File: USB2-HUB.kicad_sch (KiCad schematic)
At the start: 31 parts, among them J15 USB_OTG, J16 690-008-221-904, U12 FSUSB42MUX, U13 USB2514B-I/M2, U14 TPD4EUSB30, U15 AP22653W6, Y3 24MHz

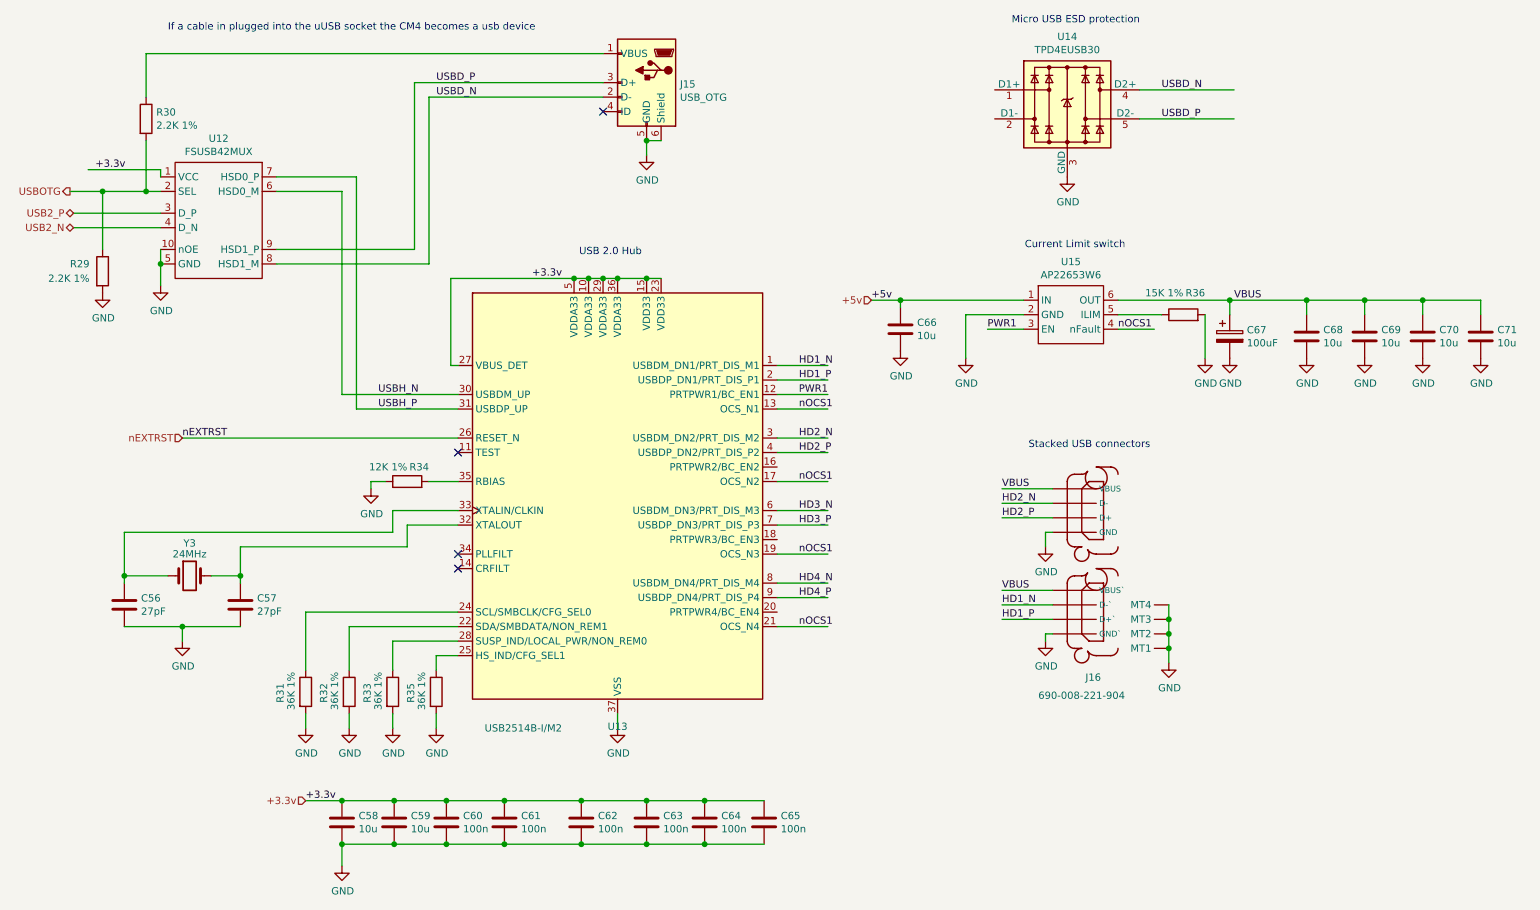
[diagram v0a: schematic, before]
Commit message: Initial layout and all parts added. Some pins still not connected to power
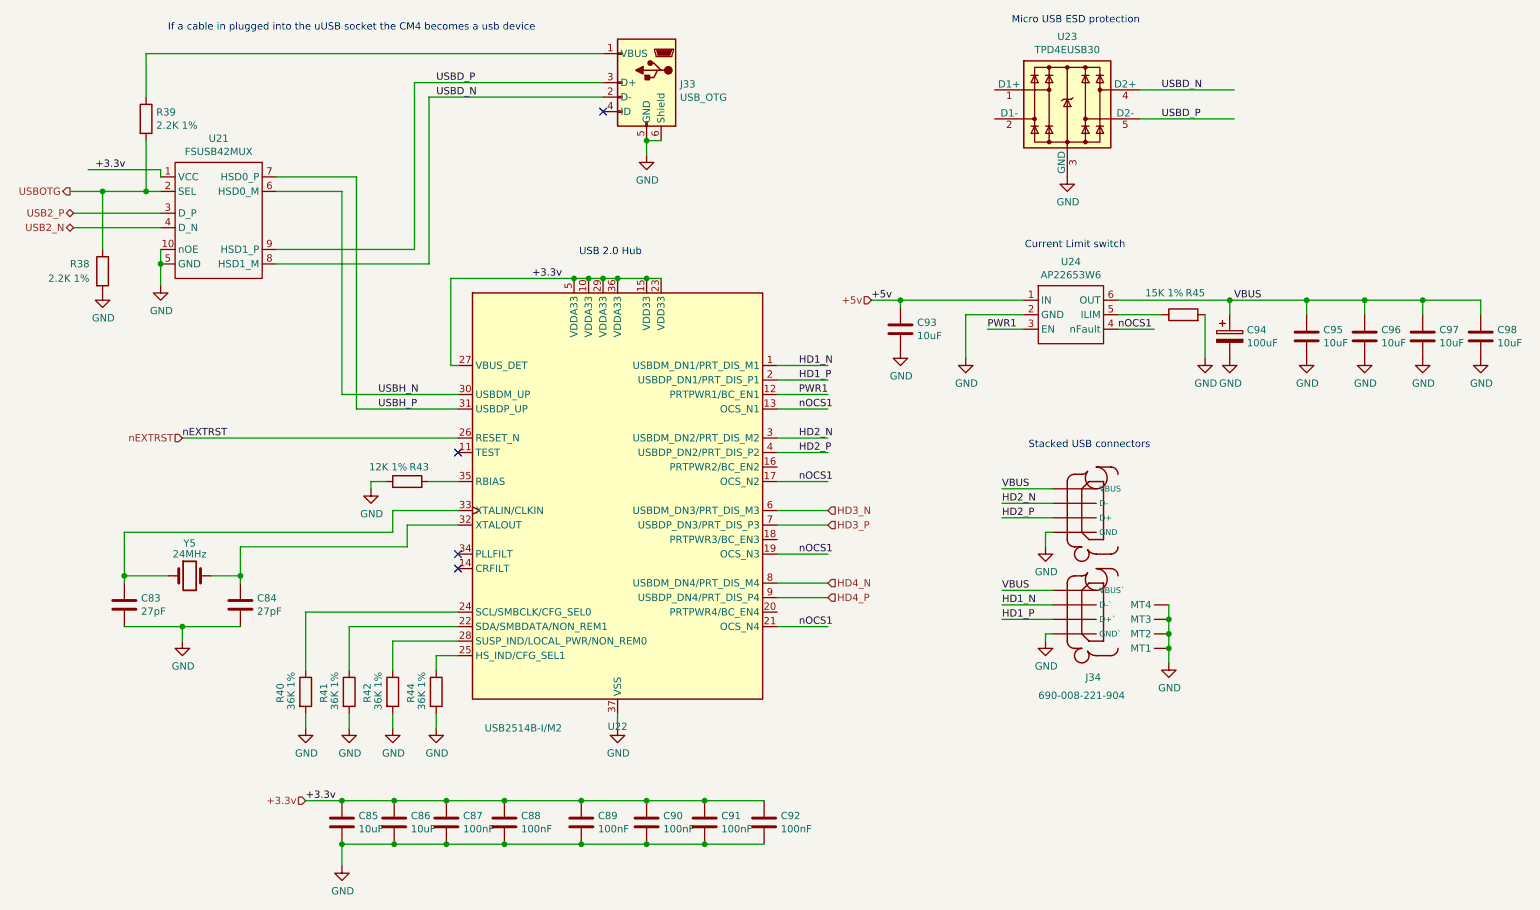
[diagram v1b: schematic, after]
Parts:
- C85: renamed from C58; value 10u -> 10uF
- C86: renamed from C59; value 10u -> 10uF
- C87: renamed from C60; value 100n -> 100nF
- C88: renamed from C61; value 100n -> 100nF
- C89: renamed from C62; value 100n -> 100nF
- C90: renamed from C63; value 100n -> 100nF
- C91: renamed from C64; value 100n -> 100nF
- C92: renamed from C65; value 100n -> 100nF
- C93: renamed from C66; value 10u -> 10uF
- C95: renamed from C68; value 10u -> 10uF
- C96: renamed from C69; value 10u -> 10uF
- C97: renamed from C70; value 10u -> 10uF
- C98: renamed from C71; value 10u -> 10uF
- Y5: renamed from Y3; footprint Crystal:Crystal_SMD_HC49-SD -> Crystal:Crystal_SMD_2012-2Pin_2.0x1.2mm
- renumbered C56 to C83, C57 to C84, C67 to C94, J15 to J33, J16 to J34, R29 to R38, R30 to R39, R31 to R40, R32 to R41, R33 to R42, R34 to R43, R35 to R44, R36 to R45, U12 to U21, U13 to U22, U14 to U23, U15 to U24

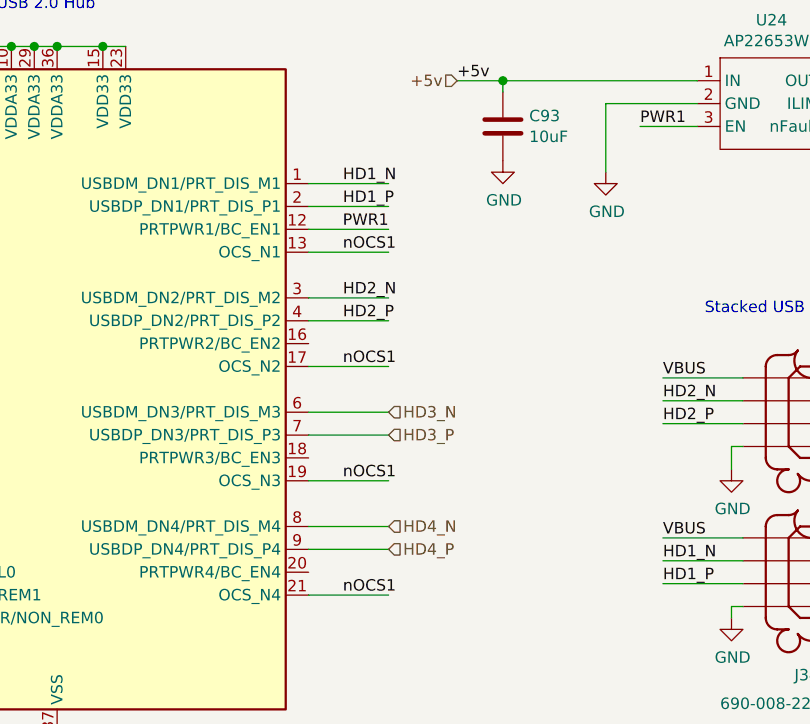
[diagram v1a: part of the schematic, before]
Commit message: Diff pairs routed
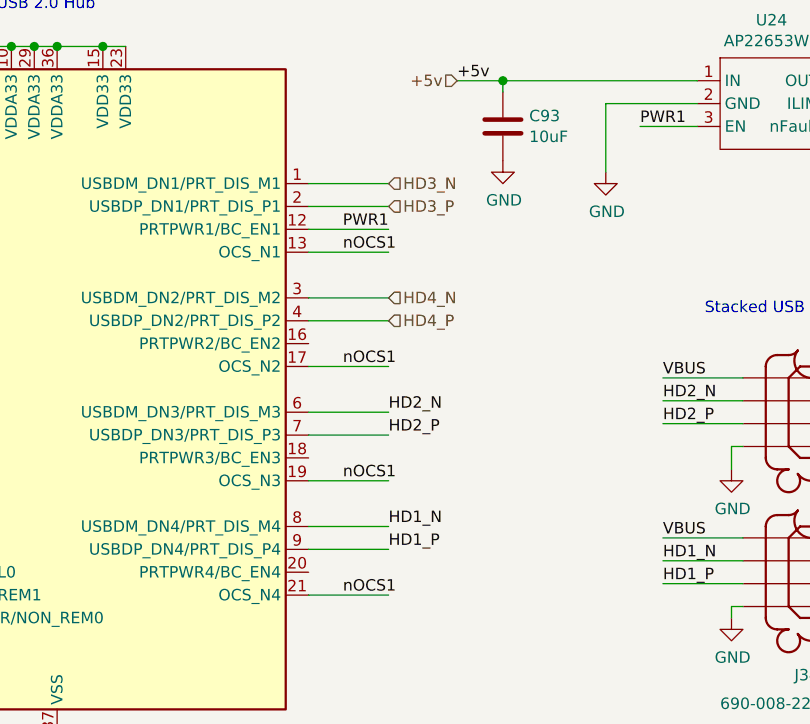
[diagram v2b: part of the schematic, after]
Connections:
- net HD1_N: now also U22.8 (USBDM_DN4/PRT_DIS_M4); no longer U22.1 (USBDM_DN1/PRT_DIS_M1)
- net HD1_P: now also U22.9 (USBDP_DN4/PRT_DIS_P4); no longer U22.2 (USBDP_DN1/PRT_DIS_P1)
- net HD2_N: now also U22.6 (USBDM_DN3/PRT_DIS_M3); no longer U22.3 (USBDM_DN2/PRT_DIS_M2)
- net HD2_P: now also U22.7 (USBDP_DN3/PRT_DIS_P3); no longer U22.4 (USBDP_DN2/PRT_DIS_P2)
- net HD3_N: now also U22.1 (USBDM_DN1/PRT_DIS_M1); no longer U22.6 (USBDM_DN3/PRT_DIS_M3)
- net HD3_P: now also U22.2 (USBDP_DN1/PRT_DIS_P1); no longer U22.7 (USBDP_DN3/PRT_DIS_P3)
- net HD4_N: now also U22.3 (USBDM_DN2/PRT_DIS_M2); no longer U22.8 (USBDM_DN4/PRT_DIS_M4)
- net HD4_P: now also U22.4 (USBDP_DN2/PRT_DIS_P2); no longer U22.9 (USBDP_DN4/PRT_DIS_P4)
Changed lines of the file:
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@@
     (comment 1 "www.raspberrypi.org")
   )
-  (junction (at 123.19 73.66) (diameter 1.016) (color 0 0 0 0))
-  (junction (at 219.71 138.43) (diameter 1.016) (color 0 0 0 0))
-  (junction (at 120.65 73.66) (diameter 1.016) (color 0 0 0 0))
-  (junction (at 84.074 172.72) (diameter 1.016) (color 0 0 0 0))
-  (junction (at 57.15 125.73) (diameter 1.016) (color 0 0 0 0))
-  (junction (at 103.378 165.1) (diameter 1.016) (color 0 0 0 0))
-  (junction (at 115.57 73.66) (diameter 1.016) (color 0 0 0 0))
   (junction (at 103.378 172.72) (diameter 1.016) (color 0 0 0 0))
-  (junction (at 128.27 49.53) (diameter 1.016) (color 0 0 0 0))
   (junction (at 138.43 172.72) (diameter 1.016) (color 0 0 0 0))
-  (junction (at 116.84 165.1) (diameter 1.016) (color 0 0 0 0))
-  (junction (at 230.378 77.47) (diameter 1.016) (color 0 0 0 0))
+  (junction (at 33.02 58.42) (diameter 1.016) (color 0 0 0 0))
+  (junction (at 74.93 165.1) (diameter 1.016) (color 0 0 0 0))
   (junction (at 254 77.47) (diameter 1.016) (color 0 0 0 0))
-  (junction (at 116.84 172.72) (diameter 1.016) (color 0 0 0 0))
-  (junction (at 74.93 172.72) (diameter 1.016) (color 0 0 0 0))
   (junction (at 138.43 165.1) (diameter 1.016) (color 0 0 0 0))
   (junction (at 219.71 133.35) (diameter 1.016) (color 0 0 0 0))
+  (junction (at 128.27 49.53) (diameter 1.016) (color 0 0 0 0))
+  (junction (at 123.19 73.66) (diameter 1.016) (color 0 0 0 0))
+  (junction (at 36.83 125.73) (diameter 1.016) (color 0 0 0 0))
+  (junction (at 120.65 73.66) (diameter 1.016) (color 0 0 0 0))
+  (junction (at 40.64 58.42) (diameter 1.016) (color 0 0 0 0))
+  (junction (at 118.11 73.66) (diameter 1.016) (color 0 0 0 0))
+  (junction (at 93.218 172.72) (diameter 1.016) (color 0 0 0 0))
+  (junction (at 128.27 165.1) (diameter 1.016) (color 0 0 0 0))
+  (junction (at 116.84 172.72) (diameter 1.016) (color 0 0 0 0))
+  (junction (at 230.378 77.47) (diameter 1.016) (color 0 0 0 0))
+  (junction (at 264.16 77.47) (diameter 1.016) (color 0 0 0 0))
+  (junction (at 74.93 172.72) (diameter 1.016) (color 0 0 0 0))
+  (junction (at 43.18 71.12) (diameter 1.016) (color 0 0 0 0))
+  (junction (at 128.27 172.72) (diameter 1.016) (color 0 0 0 0))
+  (junction (at 115.57 73.66) (diameter 1.016) (color 0 0 0 0))
+  (junction (at 93.218 165.1) (diameter 1.016) (color 0 0 0 0))
+  (junction (at 84.074 165.1) (diameter 1.016) (color 0 0 0 0))
+  (junction (at 57.15 125.73) (diameter 1.016) (color 0 0 0 0))
   (junction (at 219.71 135.89) (diameter 1.016) (color 0 0 0 0))
-  (junction (at 128.27 172.72) (diameter 1.016) (color 0 0 0 0))
-  (junction (at 74.93 165.1) (diameter 1.016) (color 0 0 0 0))
-  (junction (at 43.18 71.12) (diameter 1.016) (color 0 0 0 0))
-  (junction (at 118.11 73.66) (diameter 1.016) (color 0 0 0 0))
-  (junction (at 33.02 58.42) (diameter 1.016) (color 0 0 0 0))
-  (junction (at 84.074 165.1) (diameter 1.016) (color 0 0 0 0))
-  (junction (at 93.218 172.72) (diameter 1.016) (color 0 0 0 0))
+  (junction (at 103.378 165.1) (diameter 1.016) (color 0 0 0 0))
+  (junction (at 84.074 172.72) (diameter 1.016) (color 0 0 0 0))
+  (junction (at 219.71 138.43) (diameter 1.016) (color 0 0 0 0))
+  (junction (at 172.72 77.47) (diameter 1.016) (color 0 0 0 0))
   (junction (at 243.84 77.47) (diameter 1.016) (color 0 0 0 0))
-  (junction (at 36.83 125.73) (diameter 1.016) (color 0 0 0 0))
-  (junction (at 264.16 77.47) (diameter 1.016) (color 0 0 0 0))
-  (junction (at 40.64 58.42) (diameter 1.016) (color 0 0 0 0))
-  (junction (at 128.27 165.1) (diameter 1.016) (color 0 0 0 0))
-  (junction (at 172.72 77.47) (diameter 1.016) (color 0 0 0 0))
+  (junction (at 128.27 73.66) (diameter 1.016) (color 0 0 0 0))
   (junction (at 46.99 134.62) (diameter 1.016) (color 0 0 0 0))
-  (junction (at 93.218 165.1) (diameter 1.016) (color 0 0 0 0))
-  (junction (at 128.27 73.66) (diameter 1.016) (color 0 0 0 0))
+  (junction (at 116.84 165.1) (diameter 1.016) (color 0 0 0 0))
   (no_connect (at 95.25 121.92))
   (no_connect (at 95.25 104.14))
@@
     (effects (font (size 1.27 1.27)) (justify left bottom))
   )
-  (label "HD1_P" (at 154.94 91.44 0)
+  (label "HD1_P" (at 160.02 129.54 0)
     (effects (font (size 1.27 1.27)) (justify left bottom))
   )
@@
     (effects (font (size 1.27 1.27)) (justify left bottom))
   )
-  (label "HD1_N" (at 154.94 88.9 0)
+  (label "HD1_N" (at 160.02 127 0)
     (effects (font (size 1.27 1.27)) (justify left bottom))
   )
@@
     (effects (font (size 1.27 1.27)) (justify left bottom))
   )
-  (label "HD2_N" (at 154.94 101.6 0)
+  (label "HD2_N" (at 160.02 114.3 0)
     (effects (font (size 1.27 1.27)) (justify left bottom))
   )
@@
     (effects (font (size 1.27 1.27)) (justify left bottom))
   )
-  (label "HD2_P" (at 154.94 104.14 0)
+  (label "HD2_P" (at 160.02 116.84 0)
     (effects (font (size 1.27 1.27)) (justify left bottom))
   )
@@
     (effects (font (size 1.27 1.27)) (justify left bottom))
   )
-  (hierarchical_label "HD4_N" (shape input) (at 160.02 127 0)
+  (hierarchical_label "HD4_N" (shape input) (at 160.02 101.6 0)
     (effects (font (size 1.27 1.27)) (justify left))
   )
@@
     (effects (font (size 1.27 1.27)) (justify right))
   )
-  (hierarchical_label "HD3_P" (shape input) (at 160.02 116.84 0)
+  (hierarchical_label "HD3_P" (shape input) (at 160.02 91.44 0)
     (effects (font (size 1.27 1.27)) (justify left))
   )
@@
     (effects (font (size 1.27 1.27)) (justify right))
   )
-  (hierarchical_label "HD4_P" (shape input) (at 160.02 129.54 0)
+  (hierarchical_label "HD4_P" (shape input) (at 160.02 104.14 0)
     (effects (font (size 1.27 1.27)) (justify left))
   )
@@
     (effects (font (size 1.27 1.27)) (justify right))
   )
-  (hierarchical_label "HD3_N" (shape input) (at 160.02 114.3 0)
+  (hierarchical_label "HD3_N" (shape input) (at 160.02 88.9 0)
     (effects (font (size 1.27 1.27)) (justify left))
   )
